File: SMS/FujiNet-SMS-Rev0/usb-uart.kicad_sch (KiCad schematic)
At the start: 15 parts, among them J4 USB-C, U10 CP2102N-A02-GQFN28, U11 UMH3N

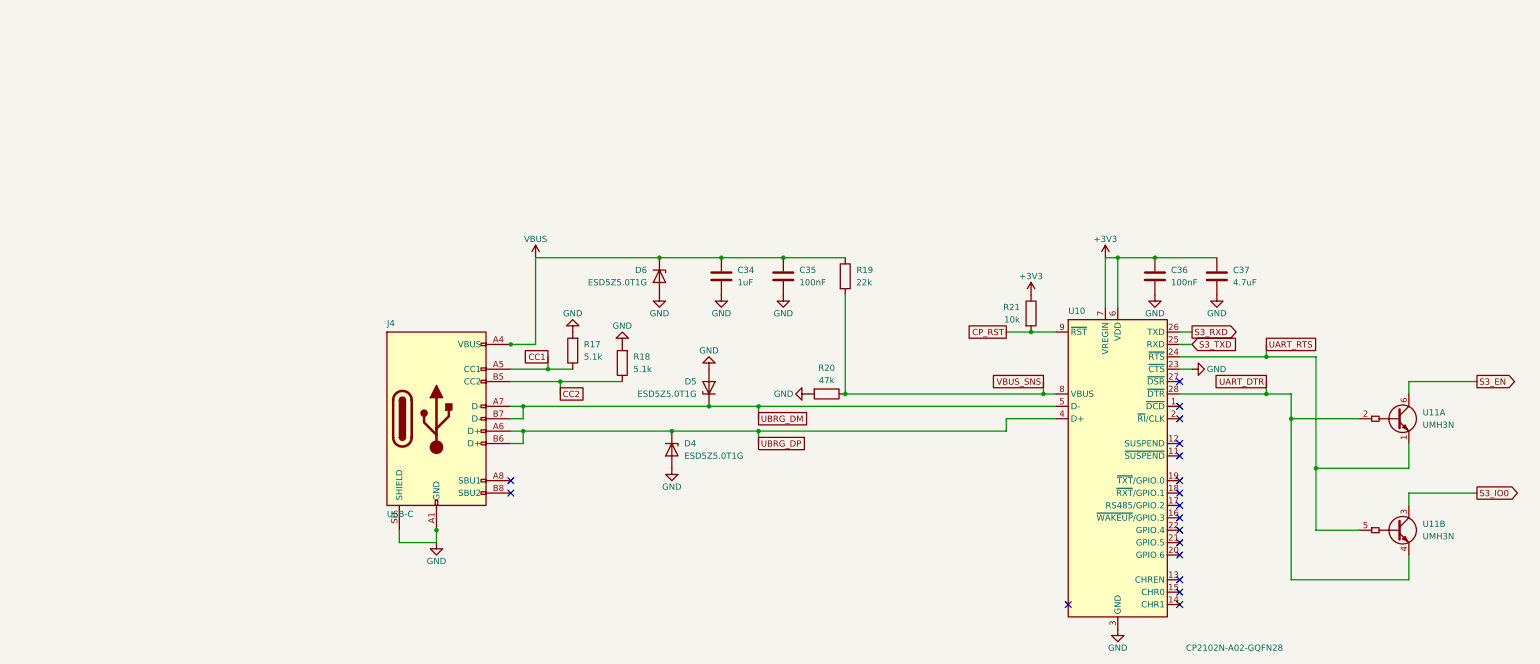
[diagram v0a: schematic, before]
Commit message: SMS Rev0: audit with kicad-happy + datasheets, fix the edge, redraw the schematic
Edge connector: every source (SMS Power slot diagram, little-scale, a 171-5519
scan, raphnet, the barbeque and reidrac footprints) puts the EVEN pins on the
component / label side with pins 1/2 at the right.  The schematic-only
footprint had the faces swapped, which would have put console +5V on /WR.
make_edge_fp.py now writes even pads on F.Cu, odd on B.Cu, 1.75 x 8.75 mm
fingers 0.75-9.5 mm from the edge on a 65.8 mm tab; check_nets.py asserts it
and tools/audit/edge_orientation.py checks it against the sources.

kicad-happy + datasheet audit (docs/design-review-rev0.md Part 1, 27 deep
review findings, gate 27/27): R_VBPD 4.7k VBUS pull-down (SS34 leakage lifts
the P-FET gate), /WAIT gate pull-up 10k -> 4.7k (GPIO34's reset pull-down vs
the 2N7002's 2.5 V threshold), 10 uF bulk on the console 5V.

Schematic: hierarchical sheets wired on a root block diagram (edge -> RP2354B
-> ESP32-S3 -> USB, glue and SRAM under the RP, power below); every sheet
drawn left to right, the glue as a wired logic network by gate depth, the
RP2354B mirrored so its bus faces the console, small sheets on A4.  Parts
are addressed by key (design.py), no more NES reference aliasing.  sch_draw
gains hierarchical labels, sheet blocks, a bus graph and flag / power-pin
lints; gen_sch checks the hierarchy against design.py and names nets by
their last path element (one bus vector per bus: KiCad joins differing
vectors by position).  ERC 0, check_nets 437/437, check_glue 8192/8192.

JLC CPL rotations measured against the EasyEDA footprint of every LCSC part
(tools/audit/jlc); the AS6C4008 has no EasyEDA footprint.

Co-Authored-By: Claude Opus 5.5 <noreply@anthropic.com>
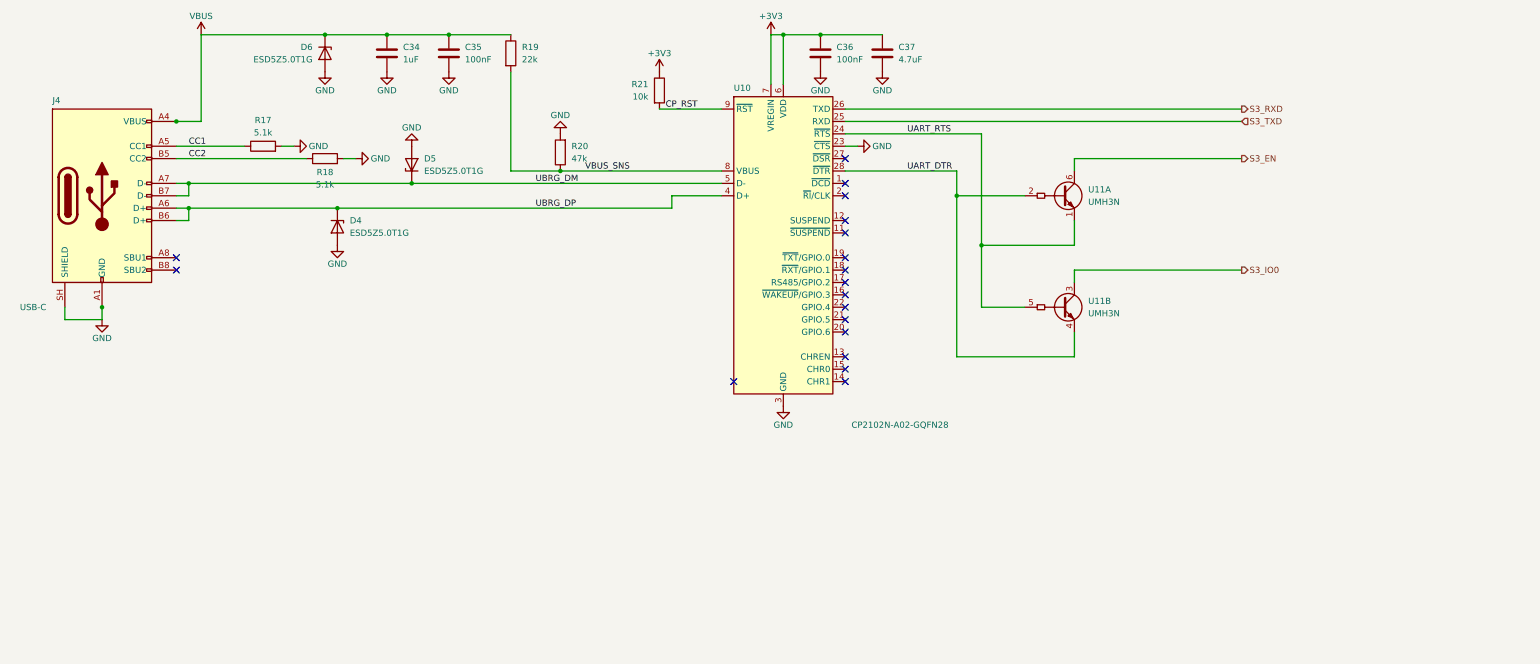
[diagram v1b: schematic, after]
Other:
- moved on the sheet: C34, C35, C36, C37, D4, D5, D6, J4, R17, R18, R19, R20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

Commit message: SMS Rev0 v2: port the FujiNet-7800 tooling, swap the near-stock-out parts
- export.py: JLCPCB and PCBWay packages (PCBWay turnkey BOM, centroid,
  assembly drawing); Manufacturer on every BOM part (design.MFR), written
  to symbols and footprints alike
- edge_geom.py: the SMS edge constants in one place (make_edge_fp,
  gen_pcb, check_gerbers); gen_pcb's body height, holes and In4 split now
  come from placement.py
- footprint paths from the schematic netlist (gen_pcb.fp_sheet_unit), so
  a part's units can be drawn on several sheets (prototype 2026-10-08:
  kicad-cli files it under the first sheet, parity accepts it)
- check_vias, check_gerbers, make_happy_config, stitch_gnd second ring,
  set_models main(), route_board.sh 12 passes / hybrid, DRC at all
  severities
- TL3342 -> TS-1187A-B-A-B (C318884), WS2812B-2020-V6 -> WS2812C-2020-V1
  (C2976072): ~5 in stock on 2026-10-07

Co-Authored-By: Claude Opus 5.5 <noreply@anthropic.com>
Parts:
- C34, C37: Manufacturer (none) -> Samsung Electro-Mechanics
- C35, C36: Manufacturer (none) -> YAGEO
- D4, D5, D6: Manufacturer (none) -> onsemi
- J4: Manufacturer (none) -> Korean Hroparts Elec
- R17, R18, R19, R20, R21: Manufacturer (none) -> UNI-ROYAL
- U10: Manufacturer (none) -> Silicon Labs
- U11: Manufacturer (none) -> Jiangsu Changjing (JSCJ)
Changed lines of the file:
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@@
+			)
+		)
+		(property "Manufacturer" "Korean Hroparts Elec"
+			(at 35.56 83.82 0)
+			(effects
+				(font
+					(size 1.27 1.27)
+				)
+				(hide yes)
 			)
 		)
@@
 			)
 		)
+		(property "Manufacturer" "onsemi"
+			(at 81.28 54.61 90)
+			(effects
+				(font
+					(size 1.27 1.27)
+				)
+				(hide yes)
+			)
+		)
 		(property "LCSC" "C82044"
 			(at 81.28 54.61 90)
@@
 			)
 		)
+		(property "Manufacturer" "Samsung Electro-Mechanics"
+			(at 93.98 54.61 0)
+			(effects
+				(font
+					(size 1.27 1.27)
+				)
+				(hide yes)
+			)
+		)
 		(property "LCSC" "C15849"
 			(at 93.98 54.61 0)
@@
 			)
 		)
+		(property "Manufacturer" "YAGEO"
+			(at 106.68 54.61 0)
+			(effects
+				(font
+					(size 1.27 1.27)
+				)
+				(hide yes)
+			)
+		)
 		(property "LCSC" "C14663"
 			(at 106.68 54.61 0)
@@
 			)
 		)
+		(property "Manufacturer" "UNI-ROYAL"
+			(at 68.58 73.66 90)
+			(effects
+				(font
+					(size 1.27 1.27)
+				)
+				(hide yes)
+			)
+		)
 		(property "LCSC" "C23186"
 			(at 68.58 73.66 90)
@@
 			)
 		)
+		(property "Manufacturer" "UNI-ROYAL"
+			(at 81.28 76.2 90)
+			(effects
+				(font
+					(size 1.27 1.27)
+				)
+				(hide yes)
+			)
+		)
 		(property "LCSC" "C23186"
 			(at 81.28 76.2 90)
@@
 			)
 		)
+		(property "Manufacturer" "Silicon Labs"
+			(at 175.26 93.98 0)
+			(effects
+				(font
+					(size 1.27 1.27)
+				)
+				(hide yes)
+			)
+		)
 		(property "LCSC" "C964632"
 			(at 175.26 93.98 0)
@@
 			)
 		)
+		(property "Manufacturer" "onsemi"
+			(at 99.06 77.47 90)
+			(effects
+				(font
+					(size 1.27 1.27)
+				)
+				(hide yes)
+			)
+		)
 		(property "LCSC" "C82044"
 			(at 99.06 77.47 90)
@@
 			)
 		)
+		(property "Manufacturer" "onsemi"
+			(at 83.82 90.17 90)
+			(effects
+				(font
+					(size 1.27 1.27)
+				)
+				(hide yes)
+			)
+		)
 		(property "LCSC" "C82044"
 			(at 83.82 90.17 90)
@@
 			)
 		)
+		(property "Manufacturer" "UNI-ROYAL"
+			(at 119.38 54.61 0)
+			(effects
+				(font
+					(size 1.27 1.27)
+				)
+				(hide yes)
+			)
+		)
 		(property "LCSC" "C31850"
 			(at 119.38 54.61 0)
@@
 			)
 		)
+		(property "Manufacturer" "UNI-ROYAL"
+			(at 129.54 74.93 0)
+			(effects
+				(font
+					(size 1.27 1.27)
+				)
+				(hide yes)
+			)
+		)
 		(property "LCSC" "C25819"
 			(at 129.54 74.93 0)
@@
 			)
 		)
+		(property "Manufacturer" "YAGEO"
+			(at 182.88 54.61 0)
+			(effects
+				(font
+					(size 1.27 1.27)
+				)
+				(hide yes)
+			)
+		)
 		(property "LCSC" "C14663"
 			(at 182.88 54.61 0)
@@
 			)
 		)
+		(property "Manufacturer" "Samsung Electro-Mechanics"
+			(at 195.58 54.61 0)
+			(effects
+				(font
+					(size 1.27 1.27)
+				)
+				(hide yes)
+			)
+		)
 		(property "LCSC" "C19666"
 			(at 195.58 54.61 0)
@@
 			)
 		)
+		(property "Manufacturer" "UNI-ROYAL"
+			(at 149.86 62.23 0)
+			(effects
+				(font
+					(size 1.27 1.27)
+				)
+				(hide yes)
+			)
+		)
 		(property "LCSC" "C25804"
 			(at 149.86 62.23 0)
@@
 			)
 		)
+		(property "Manufacturer" "Jiangsu Changjing (JSCJ)"
+			(at 233.68 83.82 0)
+			(effects
+				(font
+					(size 1.27 1.27)
+				)
+				(hide yes)
+			)
+		)
 		(property "LCSC" "C62892"
 			(at 233.68 83.82 0)
@@
 			(at 233.68 106.68 0)
 			(effects
+				(font
+					(size 1.27 1.27)
+				)
+				(hide yes)
+			)
+		)
+		(property "Manufacturer" "Jiangsu Changjing (JSCJ)"
+			(at 233.68 106.68 0)
+			(effects
